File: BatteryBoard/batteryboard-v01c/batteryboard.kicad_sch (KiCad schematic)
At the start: 30 parts, among them J1 KEYSTONE-1042, J2 KEYSTONE-1042, J3 KEYSTONE-1042, J4 KEYSTONE-1042, J5 KEYSTONE-1042, J6 KEYSTONE-1042, J7 MOLEX 5023520601, J8 Screw_Terminal_01x02, Q1 IRF7458, Q2 IRF7458, Q3 MMBT2222AT, U1 R5460N233AF

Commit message: final silkscreen and stencil edits, gerbers added for final purchase
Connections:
- net DigitalPinTBD is gone; now on net PyCubed_PA20: J7.6 (Pin_6)
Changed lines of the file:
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@@
     )
   )
-  (global_label "DigitalPinTBD" (shape input) (at 218.44 95.25 270) (fields_autoplaced)
+  (global_label "PyCubed_PA20" (shape input) (at 218.44 95.25 270) (fields_autoplaced)
     (effects (font (size 1.27 1.27)) (justify right))
-    (property "Intersheet References" "${INTERSHEET_REFS}" (id 0) (at 0 0 0)
-      (effects (font (size 1.27 1.27)) hide)
+    (property "Intersheet References" "${INTERSHEET_REFS}" (id 0) (at 218.3606 111.3628 90)
+      (effects (font (size 1.27 1.27)) (justify right) hide)
     )
   )

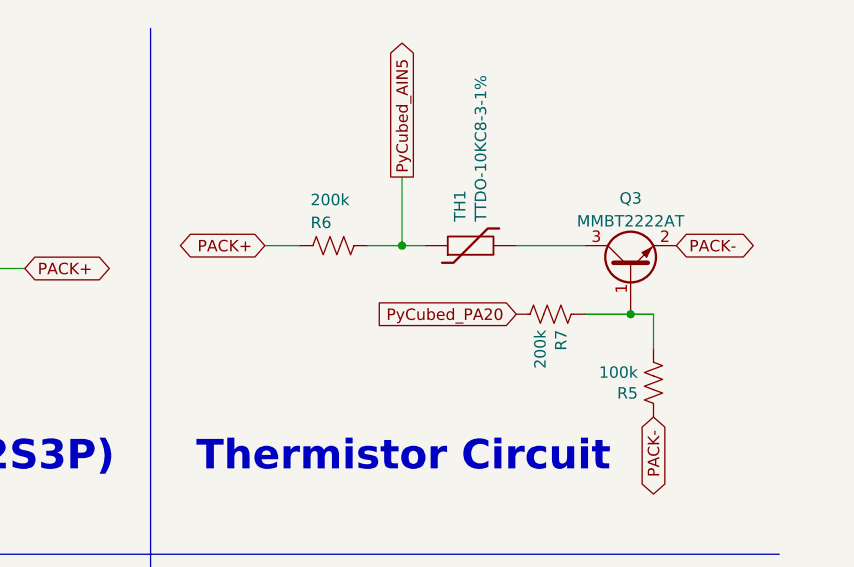
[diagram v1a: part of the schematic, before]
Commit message: final updates after JLC i2c error
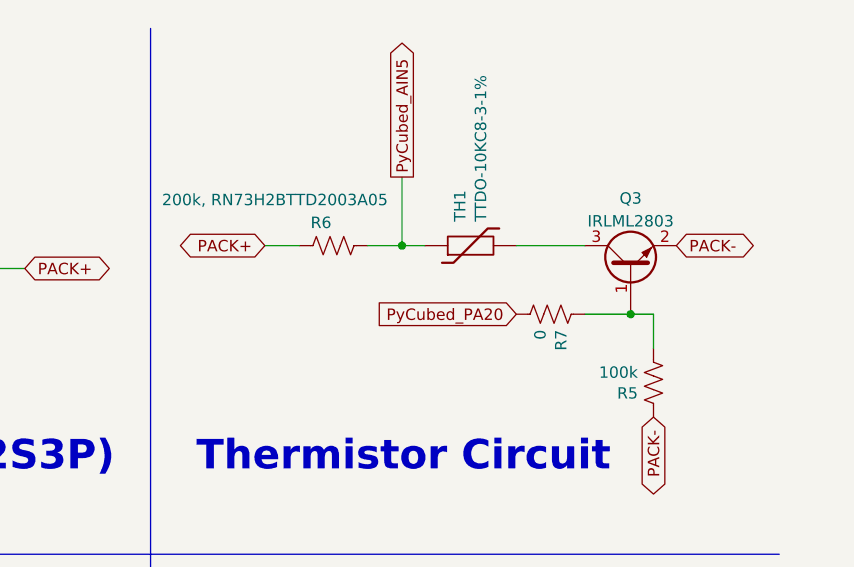
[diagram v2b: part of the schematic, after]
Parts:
- Q3: value MMBT2222AT -> IRLML2803
- R6: value 200k -> 200k, RN73H2BTTD2003A05
- R7: value 200k -> 0
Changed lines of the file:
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@@
       (effects (font (size 1.27 1.27)) (justify right))
     )
-    (property "Value" "200k" (id 1) (at 214.63 33.02 90)
+    (property "Value" "200k, RN73H2BTTD2003A05" (id 1) (at 198.12 33.02 90)
       (effects (font (size 1.27 1.27)) (justify right))
     )
@@
       (effects (font (size 1.27 1.27)) (justify right))
     )
-    (property "Value" "200k" (id 1) (at 240.157 47.4472 0)
+    (property "Value" "0" (id 1) (at 240.157 47.4472 0)
       (effects (font (size 1.27 1.27)) (justify right))
     )
@@
     (in_bom yes) (on_board yes) (fields_autoplaced)
     (property "Reference" "Q3" (id 0) (at 250.19 32.8508 90))
-    (property "Value" "MMBT2222AT" (id 1) (at 250.19 35.3877 90))
+    (property "Value" "IRLML2803" (id 1) (at 250.19 35.3877 90))
     (property "Footprint" "Package_TO_SOT_SMD:SOT-23" (id 2) (at 252.095 35.56 0)
       (effects (font (size 1.27 1.27) italic) (justify left) hide)
@@
     )
     (path "/68533814-ced2-49b8-aa44-80ce4a72751b"
-      (reference "Q3") (unit 1) (value "MMBT2222AT") (footprint "Package_TO_SOT_SMD:SOT-23")
+      (reference "Q3") (unit 1) (value "IRLML2803") (footprint "Package_TO_SOT_SMD:SOT-23")
     )
     (path "/00000000-0000-0000-0000-00005e1a611b"
@@
     )
     (path "/00000000-0000-0000-0000-00006221cab9"
-      (reference "R6") (unit 1) (value "200k") (footprint "Resistor_SMD:R_1206_3216Metric")
+      (reference "R6") (unit 1) (value "200k, RN73H2BTTD2003A05") (footprint "Resistor_SMD:R_1206_3216Metric")
     )
     (path "/00000000-0000-0000-0000-0000624cb2b4"
-      (reference "R7") (unit 1) (value "200k") (footprint "Resistor_SMD:R_0603_1608Metric")
+      (reference "R7") (unit 1) (value "0") (footprint "Resistor_SMD:R_0603_1608Metric")
     )
     (path "/00000000-0000-0000-0000-000062221bfe"
